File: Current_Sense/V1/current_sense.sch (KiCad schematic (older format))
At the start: 28 parts, among them J201 1935161, U201 LM4040CYM3-4.1-TR, U202 PGA281AIPWR, U203 ADC141S626CIMM/NOPB

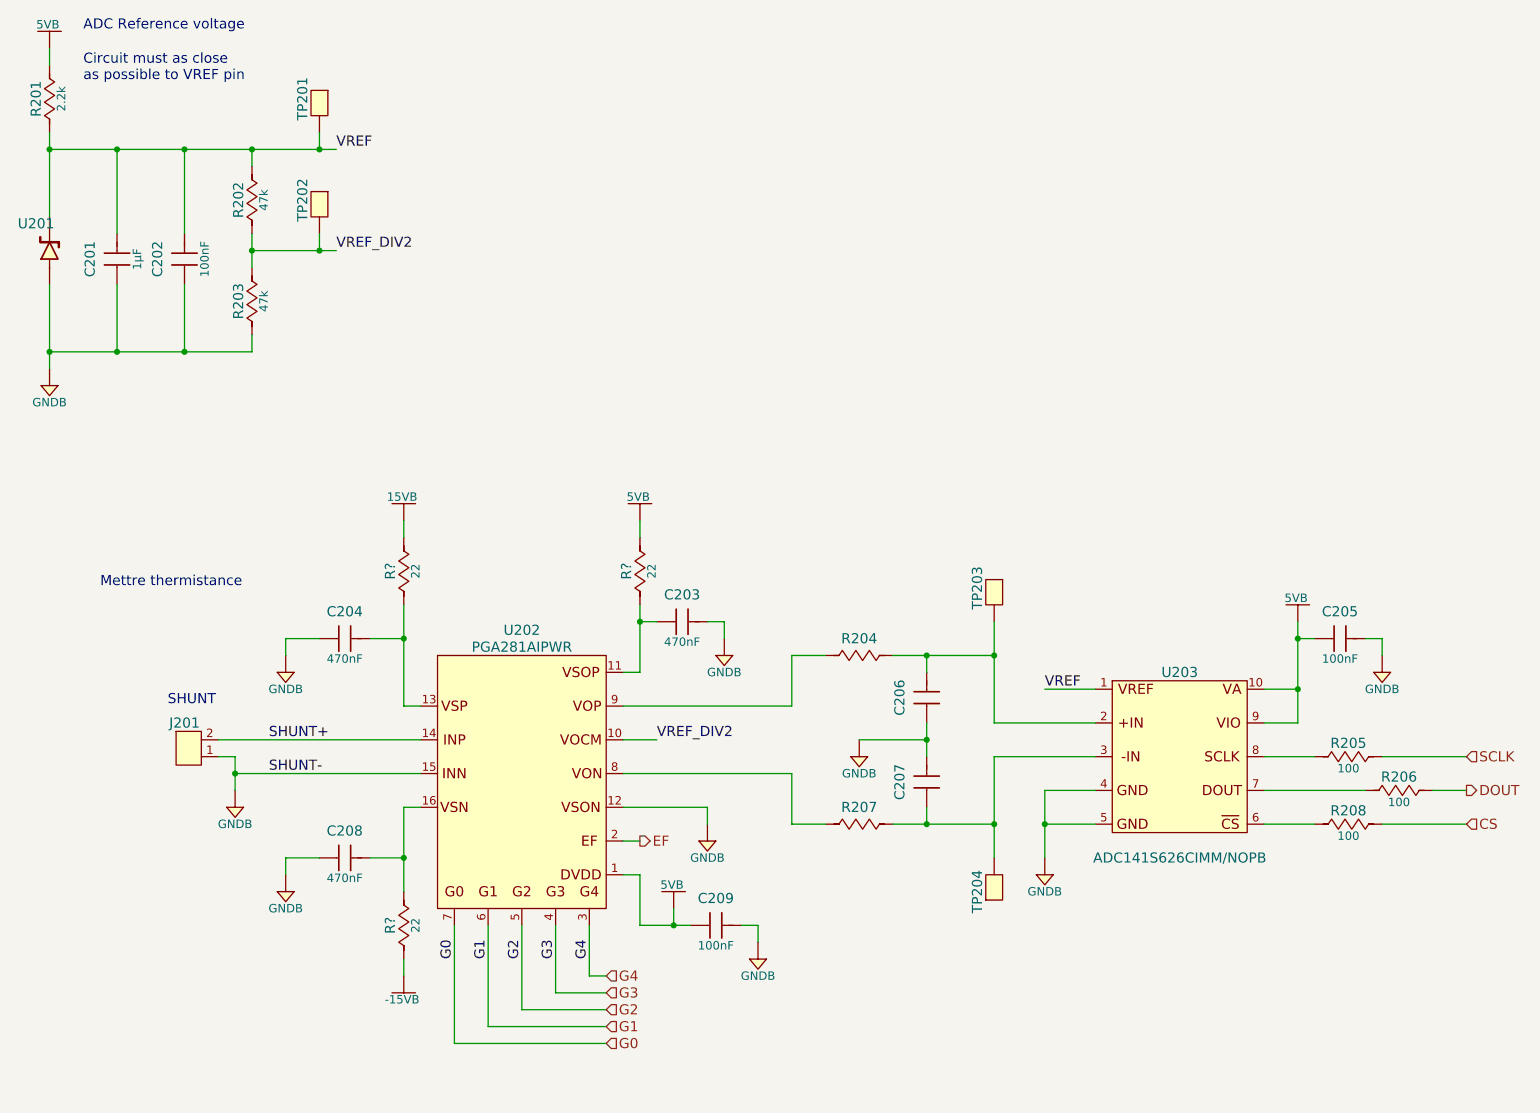
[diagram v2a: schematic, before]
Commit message: start to place pin on uC
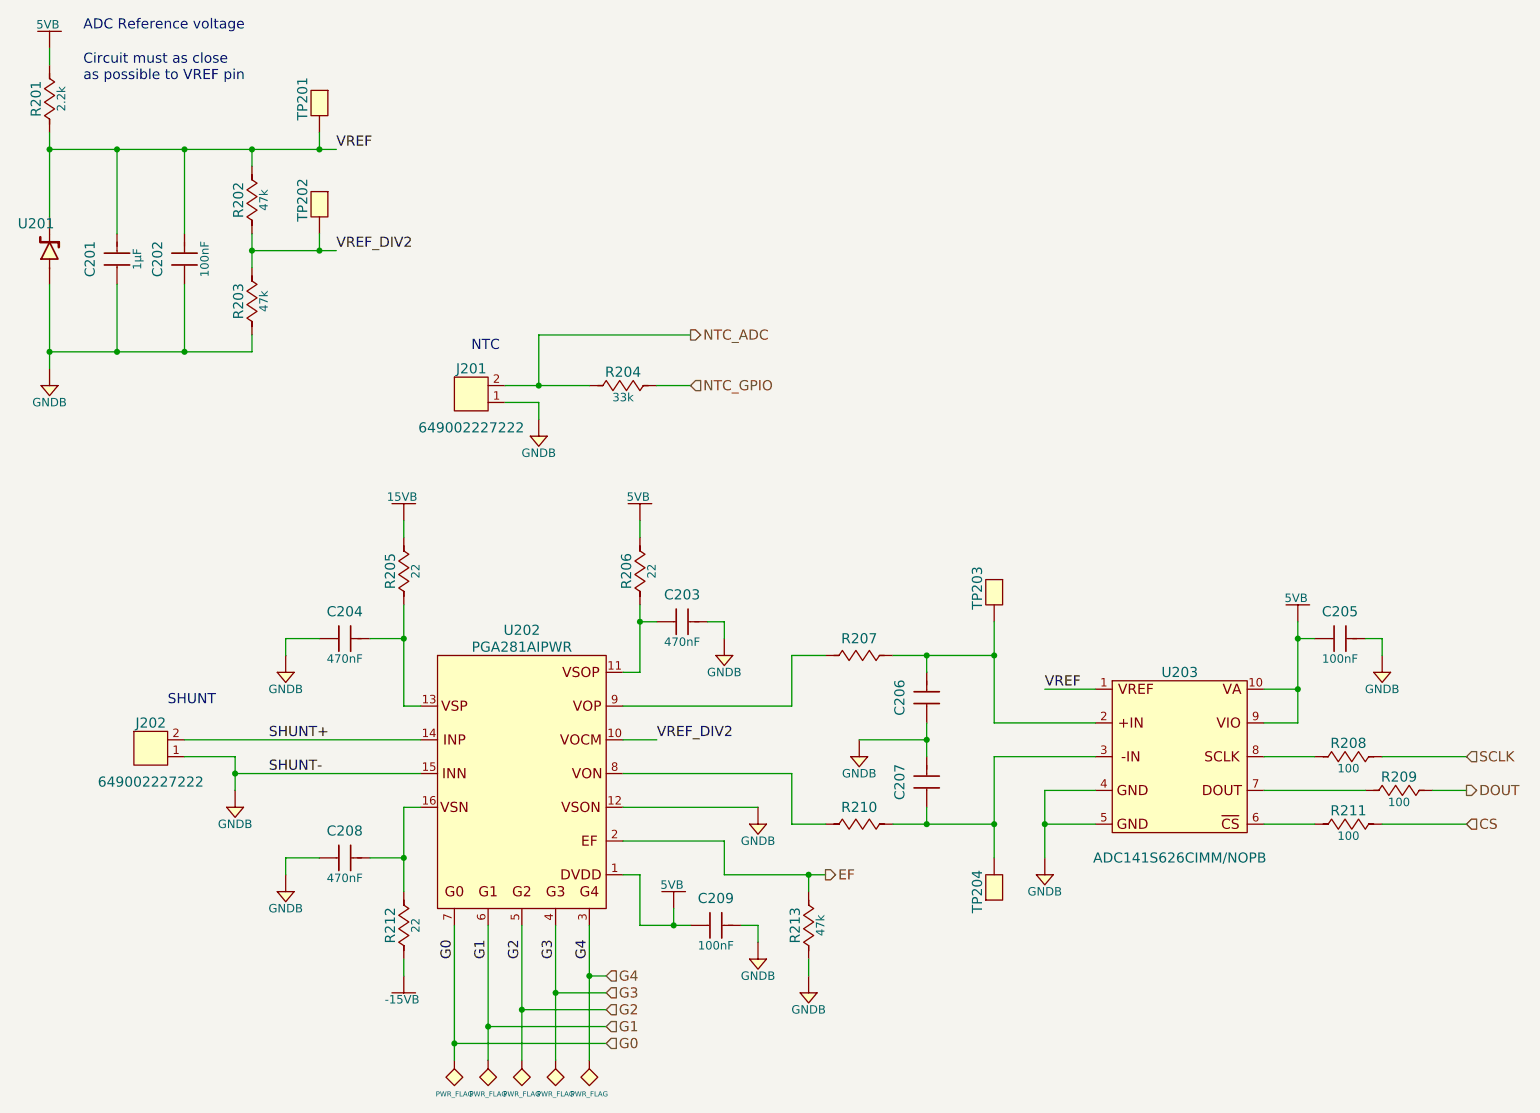
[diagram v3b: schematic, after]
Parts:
- removed J201: 1935161, Connectors:1935161, symbol 1935161
- added J201, J202: 649002227222, Connectors:649002227222, symbol 649002227222
- added R204: RC0805JR-0733KL, Resistors:R0805, symbol RC0805JR-0733KL
- added R213: RC0805JR-0747KL, Resistors:R0805, symbol RC0805JR-0747KL
- gave numbers to parts that had none: 3
- renumbered R204 to R207, R205 to R208, R206 to R209, R207 to R210, R208 to R211
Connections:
- net EF: now also R213.2
- net GNDB: now also J201.1, J202.1, R213.1
- net SHUNT+: now also J202.2
- new net NTC_ADC: J201.2, R204.1
- new net NTC_GPIO: R204.2
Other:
- note added: "NTC"
- note removed: "Mettre thermistance"

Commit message: remove NTC, place component on PCB
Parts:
- removed J201: 649002227222, Connectors:649002227222, symbol 649002227222
- removed R204: RC0805JR-0733KL, Resistors:R0805, symbol RC0805JR-0733KL
- R207, R210: footprint Capacitors:C0805 -> Resistors:R0805
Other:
- note removed: "NTC"
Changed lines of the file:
@@
 F 0 "R207" H 5800 4500 60  0000 C CNN
 F 1 "Resistor_Generic" H 5850 4100 50  0001 C CNN
-F 2 "Capacitors:C0805" H 5850 3500 30  0001 C CNN
+F 2 "Resistors:R0805" H 5850 3500 30  0001 C CNN
 F 3 "D" H 5850 3450 30  0001 C CNN
 F 4 "Supplier" H 5850 4000 60  0001 C CNN "Supplier"
@@
 F 0 "R210" H 5800 5500 60  0000 C CNN
 F 1 "Resistor_Generic" H 5850 5100 50  0001 C CNN
-F 2 "Capacitors:C0805" H 5850 4500 30  0001 C CNN
+F 2 "Resistors:R0805" H 5850 4500 30  0001 C CNN
 F 3 "D" H 5850 4450 30  0001 C CNN
 F 4 "Supplier" H 5850 5000 60  0001 C CNN "Supplier"
@@
 Wire Wire Line
 	4500 3600 4500 3700
-Text Notes 3500 2600 0    60   ~ 0
-NTC
 $Comp
 L 649002227222 J202
@@
 	1    0    0    -1
 $EndComp
-$Comp
-L 649002227222 J201
-U 1 1 595B3532
-P 3500 2900
-F 0 "J201" H 3500 3100 60  0000 C CNN
-F 1 "649002227222" H 3500 2750 60  0000 C CNN
-F 2 "Connectors:649002227222" H 3500 2000 60  0001 C CNN
-F 3 "http://katalog.we-online.de/em/datasheet/649016227222.pdf" H 3500 1900 60  0001 C CNN
-F 4 "Digikey" H 3500 2500 60  0001 C CNN "Supplier"
-F 5 "732-1937-ND" H 3500 2400 60  0001 C CNN "Supplier Part Number"
-F 6 "Wurth Electronics Inc." H 3500 2300 60  0001 C CNN "Manufacturer"
-F 7 "649002227222" H 3500 2200 60  0001 C CNN "Manufacturer Part Number"
-F 8 "HEADER MALE DUAL ANGLE W/MNT 2P" H 3500 2100 60  0001 C CNN "Description"
-	1    3500 2900
-	1    0    0    -1
-$EndComp
-$Comp
-L GNDB #PWR017
-U 1 1 595B4154
-P 3900 3100
-F 0 "#PWR017" H 3900 2930 50  0001 C CNN
-F 1 "GNDB" H 3900 3000 50  0000 C CNN
-F 2 "" H 3900 3200 60  0000 C CNN
-F 3 "" H 3880 3010 60  0000 C CNN
-	1    3900 3100
-	1    0    0    -1
-$EndComp
-Wire Wire Line
-	3700 2900 3900 2900
-Wire Wire Line
-	3900 2900 3900 3000
-Wire Wire Line
-	3700 2800 4200 2800
-$Comp
-L RC0805JR-0733KL R204
-U 1 1 595B429A
-P 4400 2800
-F 0 "R204" H 4400 2880 60  0000 C CNN
-F 1 "RC0805JR-0733KL" H 4400 2500 50  0001 C CNN
-F 2 "Resistors:R0805" H 4400 1900 30  0001 C CNN
-F 3 "http://www.yageo.com/documents/recent/PYu-RC_Group_51_RoHS_L_7.pdf" H 4400 1850 30  0001 C CNN
-F 4 "Digikey" H 4400 2400 60  0001 C CNN "Supplier"
-F 5 "311-33KARCT-ND" H 4400 2300 60  0001 C CNN "Supplier Part Number"
-F 6 "Yageo" H 4400 2200 60  0001 C CNN "Manufacturer"
-F 7 "RC0805JR-0733KL" H 4400 2100 60  0001 C CNN "Manufacturer Part Number"
-F 8 "RES SMD 33K OHM 5% 1/8W 0805" H 4400 2000 60  0001 C CNN "Description"
-F 9 "33k" H 4400 2730 50  0000 C CNN "Resistance (Ohms)"
-F 10 "±5%" H 4810 2720 50  0001 C CNN "Tolerance (%)"
-F 11 "1/8W" H 4400 2660 50  0001 C CNN "Puissance (Watts)"
-	1    4400 2800
-	1    0    0    -1
-$EndComp
-Wire Wire Line
-	4600 2800 4800 2800
-Text HLabel 4800 2800 2    60   Input ~ 0
-NTC_GPIO
-Wire Wire Line
-	3900 2800 3900 2500
-Wire Wire Line
-	3900 2500 4800 2500
-Connection ~ 3900 2800
-Text HLabel 4800 2500 2    60   Output ~ 0
-NTC_ADC
 $Comp
 L RC0805JR-0747KL R213
@@
 $EndComp
 $Comp
-L GNDB #PWR018
+L GNDB #PWR017
 U 1 1 59605E6B
 P 5500 6400
-F 0 "#PWR018" H 5500 6230 50  0001 C CNN
+F 0 "#PWR017" H 5500 6230 50  0001 C CNN
 F 1 "GNDB" H 5500 6300 50  0000 C CNN
 F 2 "" H 5500 6500 60  0000 C CNN
@@
 Connection ~ 5500 5700
 $Comp
-L PWR_FLAG #FLG019
+L PWR_FLAG #FLG018
 U 1 1 595B994C
 P 3400 6800
-F 0 "#FLG019" H 3400 6700 60  0001 C CNN
+F 0 "#FLG018" H 3400 6700 60  0001 C CNN
 F 1 "PWR_FLAG" H 3400 7000 30  0000 C CNN
 F 2 "" H 3400 6800 60  0000 C CNN
@@
 Connection ~ 3400 6700
 $Comp
-L PWR_FLAG #FLG020
+L PWR_FLAG #FLG019
 U 1 1 595BA484
 P 3800 6800
-F 0 "#FLG020" H 3800 6700 60  0001 C CNN
+F 0 "#FLG019" H 3800 6700 60  0001 C CNN
 F 1 "PWR_FLAG" H 3800 7000 30  0000 C CNN
 F 2 "" H 3800 6800 60  0000 C CNN
@@
 Connection ~ 4200 6300
 $Comp
-L PWR_FLAG #FLG021
+L PWR_FLAG #FLG020
 U 1 1 595BA607
 P 4200 6800
-F 0 "#FLG021" H 4200 6700 60  0001 C CNN
+F 0 "#FLG020" H 4200 6700 60  0001 C CNN
 F 1 "PWR_FLAG" H 4200 7000 30  0000 C CNN
 F 2 "" H 4200 6800 60  0000 C CNN
@@
 $EndComp
 $Comp
-L PWR_FLAG #FLG022
+L PWR_FLAG #FLG021
 U 1 1 595BB40E
 P 4000 6800
-F 0 "#FLG022" H 4000 6700 60  0001 C CNN
+F 0 "#FLG021" H 4000 6700 60  0001 C CNN
 F 1 "PWR_FLAG" H 4000 7000 30  0000 C CNN
 F 2 "" H 4000 6800 60  0000 C CNN
@@
 $EndComp
 $Comp
-L PWR_FLAG #FLG023
+L PWR_FLAG #FLG022
 U 1 1 595BB433
 P 3600 6800
-F 0 "#FLG023" H 3600 6700 60  0001 C CNN
+F 0 "#FLG022" H 3600 6700 60  0001 C CNN
 F 1 "PWR_FLAG" H 3600 7000 30  0000 C CNN
 F 2 "" H 3600 6800 60  0000 C CNN

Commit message: routing uC
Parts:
- removed TP203, TP204: Test_Point_THM, Connectors:Keystone_5001, symbol Test_Point_THM
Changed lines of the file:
@@
 Wire Wire Line
 	5400 5400 5600 5400
-Wire Wire Line
-	6600 4200 6600 4800
 Connection ~ 6200 4400
 Wire Wire Line
-	6600 5000 6600 5600
+	6600 5400 6600 5000
 Connection ~ 6200 5400
 Wire Wire Line
@@
 Text Label 2300 5100 0    60   ~ 0
 SHUNT-
-$Comp
-L Test_Point_THM TP203
-U 1 1 592E74C6
-P 6600 4000
-F 0 "TP203" H 6600 3900 60  0000 C CNN
-F 1 "Test_Point_THM" H 6600 3700 60  0001 C CNN
-F 2 "Connectors:Keystone_5001" H 6600 3100 60  0001 C CNN
-F 3 "http://keyelco.com/userAssets/file/M65p56.pdf" H 6600 3000 60  0001 C CNN
-F 4 "Digikey" H 6600 3600 60  0001 C CNN "Supplier"
-F 5 "36-5001-ND" H 6600 3500 60  0001 C CNN "Supplier Part Number"
-F 6 "Keystone Electronics" H 6600 3400 60  0001 C CNN "Manufacturer"
-F 7 "5001" H 6600 3300 60  0001 C CNN "Manufacturer Part Number"
-F 8 "TEST POINT PC MINI .040\"D BLACK" H 6600 3200 60  0001 C CNN "Description"
-	1    6600 4000
-	0    1    1    0
-$EndComp
 $Comp
 L Test_Point_THM TP201
@@
 $EndComp
 $Comp
-L Test_Point_THM TP204
-U 1 1 592E7654
-P 6600 5800
-F 0 "TP204" H 6600 5900 60  0000 C CNN
-F 1 "Test_Point_THM" H 6600 5500 60  0001 C CNN
-F 2 "Connectors:Keystone_5001" H 6600 4900 60  0001 C CNN
-F 3 "http://keyelco.com/userAssets/file/M65p56.pdf" H 6600 4800 60  0001 C CNN
-F 4 "Digikey" H 6600 5400 60  0001 C CNN "Supplier"
-F 5 "36-5001-ND" H 6600 5300 60  0001 C CNN "Supplier Part Number"
-F 6 "Keystone Electronics" H 6600 5200 60  0001 C CNN "Manufacturer"
-F 7 "5001" H 6600 5100 60  0001 C CNN "Manufacturer Part Number"
-F 8 "TEST POINT PC MINI .040\"D BLACK" H 6600 5000 60  0001 C CNN "Description"
-	1    6600 5800
-	0    -1   -1   0
-$EndComp
-$Comp
 L Test_Point_THM TP202
 U 1 1 592E7AF6
@@
 	2600 1300 2600 1400
 Connection ~ 2600 1400
-Connection ~ 6600 4400
-Connection ~ 6600 5400
 $Comp
 L 885012207098 C209
@@
 Connection ~ 3600 6600
 Connection ~ 4000 6400
+Wire Wire Line
+	6600 4400 6600 4800
 $EndSCHEMATC

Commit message: minor fix
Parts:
- added C210: 885012107018, Capacitors:C0805, symbol 885012107018
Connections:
- net 5VB: now also C210.1
- net GNDB: now also C210.2
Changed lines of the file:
@@
 $EndComp
 $Comp
-L 5VB #PWR01
+L 5VB #PWR201
 U 1 1 592CA773
 P 1000 800
-F 0 "#PWR01" H 1000 650 50  0001 C CNN
+F 0 "#PWR201" H 1000 650 50  0001 C CNN
 F 1 "5VB" H 990 940 50  0000 C CNN
 F 2 "" H 1000 800 60  0000 C CNN
@@
 	1000 1300 1000 1800
 $Comp
-L GNDB #PWR02
+L GNDB #PWR202
 U 1 1 592D1603
 P 1000 2800
-F 0 "#PWR02" H 1000 2630 50  0001 C CNN
+F 0 "#PWR202" H 1000 2630 50  0001 C CNN
 F 1 "GNDB" H 1000 2700 50  0000 C CNN
 F 2 "" H 1000 2900 60  0000 C CNN
@@
 $EndComp
 $Comp
-L GNDB #PWR03
+L GNDB #PWR211
 U 1 1 592D1627
 P 5200 5400
-F 0 "#PWR03" H 5200 5230 50  0001 C CNN
+F 0 "#PWR211" H 5200 5230 50  0001 C CNN
 F 1 "GNDB" H 5200 5300 50  0000 C CNN
 F 2 "" H 5200 5500 60  0000 C CNN
@@
 $EndComp
 $Comp
-L GNDB #PWR04
+L GNDB #PWR212
 U 1 1 592D1643
 P 6900 5700
-F 0 "#PWR04" H 6900 5530 50  0001 C CNN
+F 0 "#PWR212" H 6900 5530 50  0001 C CNN
 F 1 "GNDB" H 6900 5600 50  0000 C CNN
 F 2 "" H 6900 5800 60  0000 C CNN
@@
 	7200 4600 6900 4600
 $Comp
-L 5VB #PWR05
+L 5VB #PWR205
 U 1 1 592D3376
-P 8400 4200
-F 0 "#PWR05" H 8400 4050 50  0001 C CNN
-F 1 "5VB" H 8390 4340 50  0000 C CNN
-F 2 "" H 8400 4200 60  0000 C CNN
-F 3 "" H 8400 4200 60  0000 C CNN
-	1    8400 4200
-	1    0    0    -1
-$EndComp
-Wire Wire Line
-	8400 4200 8400 4800
+P 8400 3800
+F 0 "#PWR205" H 8400 3650 50  0001 C CNN
+F 1 "5VB" H 8390 3940 50  0000 C CNN
+F 2 "" H 8400 3800 60  0000 C CNN
+F 3 "" H 8400 3800 60  0000 C CNN
+	1    8400 3800
+	1    0    0    -1
+$EndComp
+Wire Wire Line
+	8400 3800 8400 4800
 Wire Wire Line
 	8400 4300 8500 4300
@@
 Connection ~ 8400 4300
 $Comp
-L GNDB #PWR06
+L GNDB #PWR208
 U 1 1 592D3453
 P 8900 4500
-F 0 "#PWR06" H 8900 4330 50  0001 C CNN
+F 0 "#PWR208" H 8900 4330 50  0001 C CNN
 F 1 "GNDB" H 8900 4400 50  0000 C CNN
 F 2 "" H 8900 4600 60  0000 C CNN
@@
 	8800 4300 8900 4300
 Wire Wire Line
-	8900 4300 8900 4400
+	8900 3900 8900 4400
 Wire Wire Line
 	8400 4600 8200 4600
@@
 	8900 5400 9400 5400
 $Comp
-L 5VB #PWR07
+L 5VB #PWR204
 U 1 1 592E5071
 P 4500 3600
-F 0 "#PWR07" H 4500 3450 50  0001 C CNN
+F 0 "#PWR204" H 4500 3450 50  0001 C CNN
 F 1 "5VB" H 4490 3740 50  0000 C CNN
 F 2 "" H 4500 3600 60  0000 C CNN
@@
 Connection ~ 4500 4200
 $Comp
-L GNDB #PWR08
+L GNDB #PWR206
 U 1 1 592E531D
 P 5000 4400
-F 0 "#PWR08" H 5000 4230 50  0001 C CNN
+F 0 "#PWR206" H 5000 4230 50  0001 C CNN
 F 1 "GNDB" H 5000 4300 50  0000 C CNN
 F 2 "" H 5000 4500 60  0000 C CNN
@@
 	4400 5300 5200 5300
 $Comp
-L GNDB #PWR09
+L GNDB #PWR213
 U 1 1 592E57F9
 P 2400 5800
-F 0 "#PWR09" H 2400 5630 50  0001 C CNN
+F 0 "#PWR213" H 2400 5630 50  0001 C CNN
 F 1 "GNDB" H 2400 5700 50  0000 C CNN
 F 2 "" H 2400 5900 60  0000 C CNN
@@
 	2400 5600 2600 5600
 $Comp
-L -15VB #PWR010
+L -15VB #PWR216
 U 1 1 592E5864
 P 3100 6300
-F 0 "#PWR010" H 3100 6020 50  0001 C CNN
+F 0 "#PWR216" H 3100 6020 50  0001 C CNN
 F 1 "-15VB" H 3090 6160 50  0000 C CNN
 F 2 "" H 3100 6300 60  0000 C CNN
@@
 Connection ~ 3100 5600
 $Comp
-L GNDB #PWR011
+L GNDB #PWR207
 U 1 1 592E5AAF
 P 2400 4500
-F 0 "#PWR011" H 2400 4330 50  0001 C CNN
+F 0 "#PWR207" H 2400 4330 50  0001 C CNN
 F 1 "GNDB" H 2400 4400 50  0000 C CNN
 F 2 "" H 2400 4600 60  0000 C CNN
@@
 	2400 4300 2600 4300
 $Comp
-L 15VB #PWR012
+L 15VB #PWR203
 U 1 1 592E5ACE
 P 3100 3600
-F 0 "#PWR012" H 3100 3450 50  0001 C CNN
+F 0 "#PWR203" H 3100 3450 50  0001 C CNN
 F 1 "15VB" H 3090 3740 50  0000 C CNN
 F 2 "" H 3100 3600 60  0000 C CNN
@@
 $EndComp
 $Comp
-L GNDB #PWR013
+L GNDB #PWR209
 U 1 1 592E621F
 P 5800 5000
-F 0 "#PWR013" H 5800 4830 50  0001 C CNN
+F 0 "#PWR209" H 5800 4830 50  0001 C CNN
 F 1 "GNDB" H 5800 4900 50  0000 C CNN
 F 2 "" H 5800 5100 60  0000 C CNN
@@
 	6600 5000 7200 5000
 $Comp
-L GNDB #PWR014
+L GNDB #PWR210
 U 1 1 592E6FFE
 P 2100 5300
-F 0 "#PWR014" H 2100 5130 50  0001 C CNN
+F 0 "#PWR210" H 2100 5130 50  0001 C CNN
 F 1 "GNDB" H 2100 5200 50  0000 C CNN
 F 2 "" H 2100 5400 60  0000 C CNN
@@
 	4500 6000 4800 6000
 $Comp
-L GNDB #PWR015
+L GNDB #PWR215
 U 1 1 592EDD4F
 P 5200 6200
-F 0 "#PWR015" H 5200 6030 50  0001 C CNN
+F 0 "#PWR215" H 5200 6030 50  0001 C CNN
 F 1 "GNDB" H 5200 6100 50  0000 C CNN
 F 2 "" H 5200 6300 60  0000 C CNN
@@
 	5200 6000 5200 6100
 $Comp
-L 5VB #PWR016
+L 5VB #PWR214
 U 1 1 592EDD91
 P 4700 5900
-F 0 "#PWR016" H 4700 5750 50  0001 C CNN
+F 0 "#PWR214" H 4700 5750 50  0001 C CNN
 F 1 "5VB" H 4690 6040 50  0000 C CNN
 F 2 "" H 4700 5900 60  0000 C CNN
@@
 $EndComp
 $Comp
-L GNDB #PWR017
+L GNDB #PWR217
 U 1 1 59605E6B
 P 5500 6400
-F 0 "#PWR017" H 5500 6230 50  0001 C CNN
+F 0 "#PWR217" H 5500 6230 50  0001 C CNN
 F 1 "GNDB" H 5500 6300 50  0000 C CNN
 F 2 "" H 5500 6500 60  0000 C CNN
@@
 Connection ~ 5500 5700
 $Comp
-L PWR_FLAG #FLG018
+L PWR_FLAG #FLG201
 U 1 1 595B994C
 P 3400 6800
-F 0 "#FLG018" H 3400 6700 60  0001 C CNN
+F 0 "#FLG201" H 3400 6700 60  0001 C CNN
 F 1 "PWR_FLAG" H 3400 7000 30  0000 C CNN
 F 2 "" H 3400 6800 60  0000 C CNN
@@
 Connection ~ 3400 6700
 $Comp
-L PWR_FLAG #FLG019
+L PWR_FLAG #FLG203
 U 1 1 595BA484
 P 3800 6800
-F 0 "#FLG019" H 3800 6700 60  0001 C CNN
+F 0 "#FLG203" H 3800 6700 60  0001 C CNN
 F 1 "PWR_FLAG" H 3800 7000 30  0000 C CNN
 F 2 "" H 3800 6800 60  0000 C CNN
@@
 Connection ~ 4200 6300
 $Comp
-L PWR_FLAG #FLG020
+L PWR_FLAG #FLG205
 U 1 1 595BA607
 P 4200 6800
-F 0 "#FLG020" H 4200 6700 60  0001 C CNN
+F 0 "#FLG205" H 4200 6700 60  0001 C CNN
 F 1 "PWR_FLAG" H 4200 7000 30  0000 C CNN
 F 2 "" H 4200 6800 60  0000 C CNN
@@
 $EndComp
 $Comp
-L PWR_FLAG #FLG021
+L PWR_FLAG #FLG204
 U 1 1 595BB40E
 P 4000 6800
-F 0 "#FLG021" H 4000 6700 60  0001 C CNN
+F 0 "#FLG204" H 4000 6700 60  0001 C CNN
 F 1 "PWR_FLAG" H 4000 7000 30  0000 C CNN
 F 2 "" H 4000 6800 60  0000 C CNN
@@
 $EndComp
 $Comp
-L PWR_FLAG #FLG022
+L PWR_FLAG #FLG202
 U 1 1 595BB433
 P 3600 6800
-F 0 "#FLG022" H 3600 6700 60  0001 C CNN
+F 0 "#FLG202" H 3600 6700 60  0001 C CNN
 F 1 "PWR_FLAG" H 3600 7000 30  0000 C CNN
 F 2 "" H 3600 6800 60  0000 C CNN
@@
 Wire Wire Line
 	6600 4400 6600 4800
+$Comp
+L 885012107018 C210
+U 1 1 595E6777
+P 8700 3900
+F 0 "C210" H 8650 4060 60  0000 C CNN
+F 1 "885012107018" H 8650 3550 60  0001 C CNN
+F 2 "Capacitors:C0805" H 8650 2950 60  0001 C CNN
+F 3 "D" H 8650 2850 60  0001 C CNN
+F 4 "Digikey" H 8650 3450 60  0001 C CNN "Supplier"
+F 5 "732-7628-1-ND" H 8650 3350 60  0001 C CNN "Supplier Part Number"
+F 6 "Wurth Electronics Inc." H 8650 3250 60  0001 C CNN "Manufacturer"
+F 7 "885012107018" H 8650 3150 60  0001 C CNN "Manufacturer Part Number"
+F 8 "CAP CER 4.7UF 25V X5R 0805" H 8650 3050 60  0001 C CNN "Description"
+F 9 "4.7µF" H 8650 3780 50  0000 C CNN "Capacitance (Farad)"
+F 10 "±20%" H 8910 3780 50  0001 C CNN "Tolerance (%)"
+F 11 "25V" H 8650 3710 50  0001 C CNN "Voltage Rated (Volt)"
+	1    8700 3900
+	1    0    0    -1
+$EndComp
+Wire Wire Line
+	8500 3900 8400 3900
+Connection ~ 8400 3900
+Wire Wire Line
+	8800 3900 8900 3900
+Connection ~ 8900 4300
 $EndSCHEMATC

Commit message: add note
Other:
- note added: "33k"
- note added: "470pF"
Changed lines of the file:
@@
 	8800 3900 8900 3900
 Connection ~ 8900 4300
+Text Notes 5800 5600 0    60   ~ 0
+33k
+Text Notes 5700 4600 0    60   ~ 0
+33k
+Text Notes 6300 4600 0    60   ~ 0
+470pF
+Text Notes 6300 5100 0    60   ~ 0
+470pF
 $EndSCHEMATC
